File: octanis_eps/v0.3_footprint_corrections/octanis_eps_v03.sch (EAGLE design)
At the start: 100 parts, among them IC1 OPA2333DGK, IC5 OPA2333DGK, IC7 OPA2333DGK, IC9 OPA2333DGK, Q1 FC-12M, Q2 N-HEXFET-2D_SOT232-, Q3 N-HEXFET-2D_SOT232-, Q4 N-HEXFET-2D_SOT232-

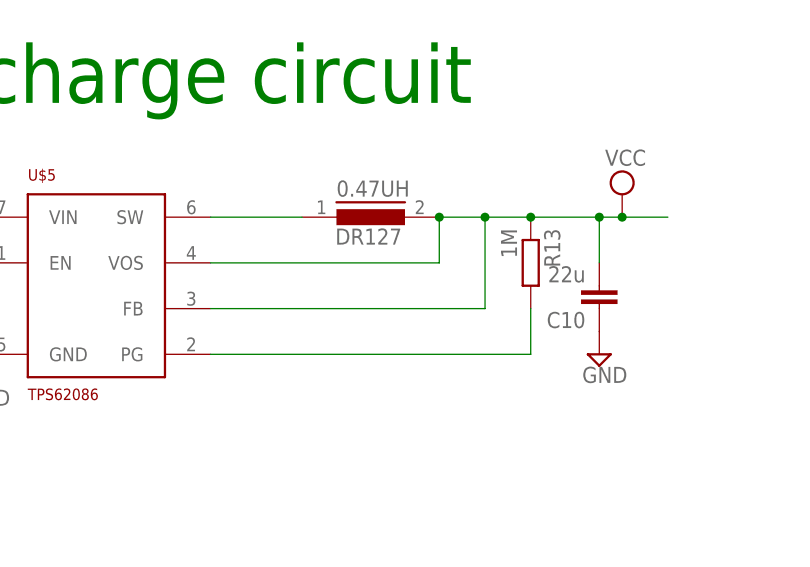
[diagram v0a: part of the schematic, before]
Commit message: corrected footprints for MSP & Step down, 50mOhms still to be changed (4points probe)
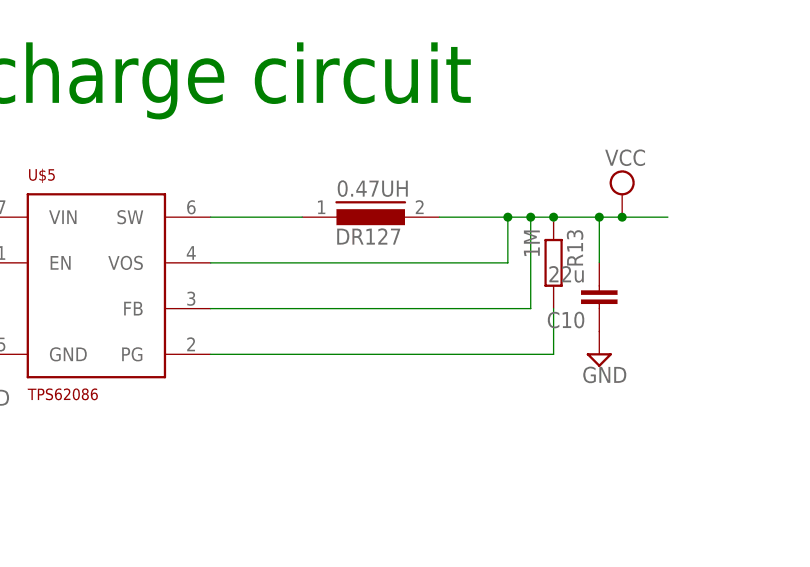
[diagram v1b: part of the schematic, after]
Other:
- moved on the sheet: R13
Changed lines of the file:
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@@
 <layer number="51" name="tDocu" color="7" fill="1" visible="no" active="no"/>
 <layer number="52" name="bDocu" color="7" fill="1" visible="no" active="no"/>
+<layer number="53" name="tGND_GNDA" color="7" fill="9" visible="no" active="no"/>
+<layer number="54" name="bGND_GNDA" color="1" fill="9" visible="no" active="no"/>
+<layer number="56" name="wert" color="7" fill="1" visible="no" active="no"/>
 <layer number="90" name="Modules" color="5" fill="1" visible="yes" active="yes"/>
 <layer number="91" name="Nets" color="2" fill="1" visible="yes" active="yes"/>
@@
 <layer number="109" name="fp9" color="7" fill="1" visible="yes" active="yes"/>
 <layer number="110" name="fp0" color="7" fill="1" visible="yes" active="yes"/>
+<layer number="111" name="LPC17xx" color="7" fill="1" visible="yes" active="yes"/>
+<layer number="112" name="tSilk" color="7" fill="1" visible="yes" active="yes"/>
 <layer number="116" name="Patch_BOT" color="9" fill="4" visible="yes" active="yes"/>
 <layer number="121" name="tTestdril" color="7" fill="1" visible="yes" active="yes"/>
@@
 <layer number="123" name="tTestmark" color="7" fill="1" visible="yes" active="yes"/>
 <layer number="124" name="bTestmark" color="7" fill="1" visible="yes" active="yes"/>
+<layer number="125" name="_tNames" color="7" fill="1" visible="yes" active="yes"/>
+<layer number="126" name="_bNames" color="7" fill="1" visible="yes" active="yes"/>
+<layer number="127" name="_tValues" color="7" fill="1" visible="yes" active="yes"/>
+<layer number="128" name="_bValues" color="7" fill="1" visible="yes" active="yes"/>
 <layer number="131" name="tAdjust" color="7" fill="1" visible="yes" active="yes"/>
 <layer number="132" name="bAdjust" color="7" fill="1" visible="yes" active="yes"/>
+<layer number="144" name="Drill_legend" color="7" fill="1" visible="yes" active="yes"/>
+<layer number="151" name="HeatSink" color="7" fill="1" visible="yes" active="yes"/>
+<layer number="152" name="_bDocu" color="7" fill="1" visible="yes" active="yes"/>
+<layer number="199" name="Contour" color="7" fill="1" visible="yes" active="yes"/>
 <layer number="200" name="200bmp" color="7" fill="1" visible="yes" active="yes"/>
 <layer number="201" name="201bmp" color="7" fill="1" visible="yes" active="yes"/>
@@
 <layer number="209" name="209bmp" color="7" fill="1" visible="yes" active="yes"/>
 <layer number="210" name="210bmp" color="7" fill="1" visible="yes" active="yes"/>
+<layer number="211" name="211bmp" color="7" fill="1" visible="yes" active="yes"/>
+<layer number="212" name="212bmp" color="7" fill="1" visible="yes" active="yes"/>
+<layer number="213" name="213bmp" color="7" fill="1" visible="yes" active="yes"/>
+<layer number="214" name="214bmp" color="7" fill="1" visible="yes" active="yes"/>
+<layer number="215" name="215bmp" color="7" fill="1" visible="yes" active="yes"/>
+<layer number="216" name="216bmp" color="7" fill="1" visible="yes" active="yes"/>
+<layer number="217" name="217bmp" color="18" fill="1" visible="no" active="no"/>
+<layer number="218" name="218bmp" color="19" fill="1" visible="no" active="no"/>
+<layer number="219" name="219bmp" color="20" fill="1" visible="no" active="no"/>
+<layer number="220" name="220bmp" color="21" fill="1" visible="no" active="no"/>
+<layer number="221" name="221bmp" color="22" fill="1" visible="no" active="no"/>
+<layer number="222" name="222bmp" color="23" fill="1" visible="no" active="no"/>
+<layer number="223" name="223bmp" color="24" fill="1" visible="no" active="no"/>
+<layer number="224" name="224bmp" color="25" fill="1" visible="no" active="no"/>
+<layer number="248" name="Housing" color="7" fill="1" visible="yes" active="yes"/>
+<layer number="249" name="Edge" color="7" fill="1" visible="yes" active="yes"/>
 <layer number="250" name="Descript" color="3" fill="1" visible="no" active="no"/>
 <layer number="251" name="SMDround" color="12" fill="11" visible="no" active="no"/>
@@
 <instance part="R11" gate="G$1" x="177.8" y="-182.88" rot="R180"/>
 <instance part="R12" gate="G$1" x="165.1" y="-167.64" rot="R270"/>
-<instance part="R13" gate="G$1" x="373.38" y="-167.64" rot="R270"/>
+<instance part="R13" gate="G$1" x="375.92" y="-167.64" rot="R270"/>
 <instance part="C4" gate="G$1" x="88.9" y="-177.8" rot="R180"/>
 <instance part="C5" gate="G$1" x="157.48" y="-193.04" rot="R180"/>
@@
 </segment>
 <segment>
-<pinref part="U$5" gate="G$1" pin="VOS"/>
-<wire x1="337.82" y1="-167.64" x2="363.22" y2="-167.64" width="0.1524" layer="91"/>
-<wire x1="363.22" y1="-167.64" x2="363.22" y2="-162.56" width="0.1524" layer="91"/>
 <pinref part="U$5" gate="G$1" pin="FB"/>
-<wire x1="337.82" y1="-172.72" x2="368.3" y2="-172.72" width="0.1524" layer="91"/>
-<wire x1="368.3" y1="-172.72" x2="368.3" y2="-162.56" width="0.1524" layer="91"/>
-<wire x1="368.3" y1="-162.56" x2="363.22" y2="-162.56" width="0.1524" layer="91"/>
-<wire x1="368.3" y1="-162.56" x2="373.38" y2="-162.56" width="0.1524" layer="91"/>
-<junction x="368.3" y="-162.56"/>
+<wire x1="337.82" y1="-172.72" x2="373.38" y2="-172.72" width="0.1524" layer="91"/>
+<wire x1="373.38" y1="-172.72" x2="373.38" y2="-162.56" width="0.1524" layer="91"/>
+<wire x1="373.38" y1="-162.56" x2="370.84" y2="-162.56" width="0.1524" layer="91"/>
+<wire x1="370.84" y1="-162.56" x2="363.22" y2="-162.56" width="0.1524" layer="91"/>
+<wire x1="373.38" y1="-162.56" x2="375.92" y2="-162.56" width="0.1524" layer="91"/>
+<junction x="373.38" y="-162.56"/>
 <pinref part="C10" gate="G$1" pin="2"/>
-<wire x1="373.38" y1="-162.56" x2="381" y2="-162.56" width="0.1524" layer="91"/>
+<wire x1="375.92" y1="-162.56" x2="381" y2="-162.56" width="0.1524" layer="91"/>
 <wire x1="381" y1="-167.64" x2="381" y2="-162.56" width="0.1524" layer="91"/>
 <wire x1="381" y1="-162.56" x2="383.54" y2="-162.56" width="0.1524" layer="91"/>
@@
 <junction x="383.54" y="-162.56"/>
 <pinref part="R13" gate="G$1" pin="1"/>
-<junction x="373.38" y="-162.56"/>
+<junction x="375.92" y="-162.56"/>
 <pinref part="0.47UH" gate="G$1" pin="2"/>
-<junction x="363.22" y="-162.56"/>
+<pinref part="U$5" gate="G$1" pin="VOS"/>
+<wire x1="337.82" y1="-167.64" x2="370.84" y2="-167.64" width="0.1524" layer="91"/>
+<wire x1="370.84" y1="-167.64" x2="370.84" y2="-162.56" width="0.1524" layer="91"/>
+<junction x="370.84" y="-162.56"/>
 </segment>
 <segment>
@@
 <pinref part="U$5" gate="G$1" pin="PG"/>
 <pinref part="R13" gate="G$1" pin="2"/>
-<wire x1="337.82" y1="-177.8" x2="373.38" y2="-177.8" width="0.1524" layer="91"/>
-<wire x1="373.38" y1="-177.8" x2="373.38" y2="-172.72" width="0.1524" layer="91"/>
-</segment>
-</net>
+<wire x1="337.82" y1="-177.8" x2="375.92" y2="-177.8" width="0.1524" layer="91"/>
+<wire x1="375.92" y1="-177.8" x2="375.92" y2="-172.72" width="0.1524" layer="91"/>
+</segment>
+</net>

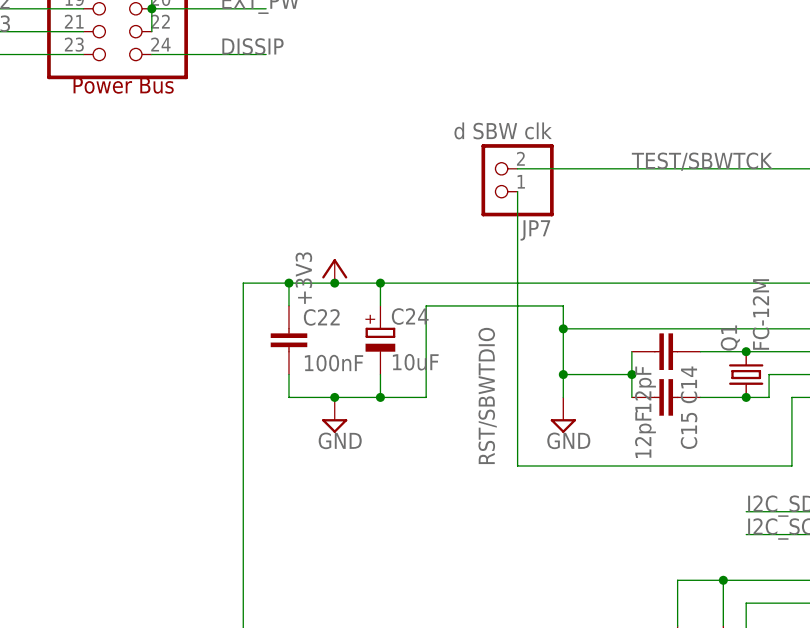
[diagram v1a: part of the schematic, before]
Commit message: pull-up on RST, need to modify the current sensor pads
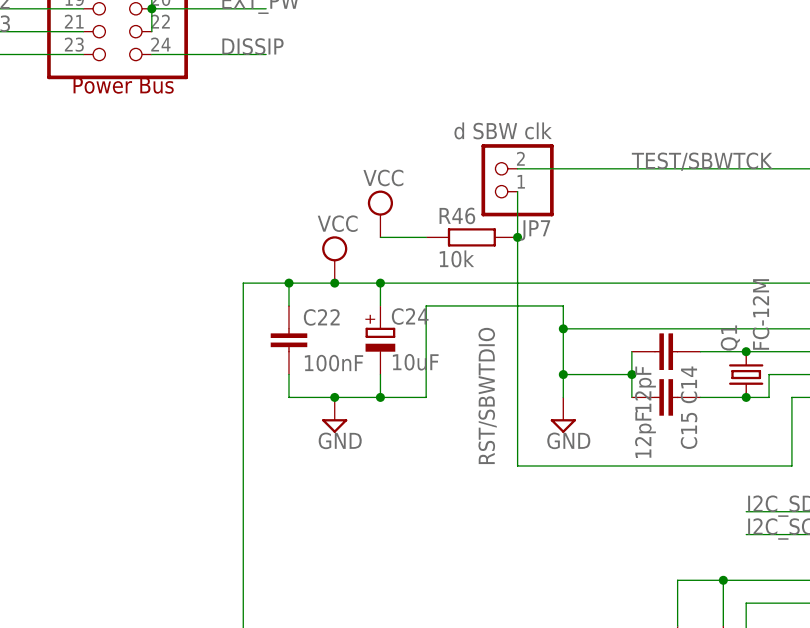
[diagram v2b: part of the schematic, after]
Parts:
- added R46: 10k, rcl:R-EU_R0603
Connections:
- removed net +3V3: C22.1, C24.+, FERRITE_BEAD.1, U$6.DVCC
- net RST/SBWTDIO: now also R46.2
- net VCC: now also C22.1, C24.+, FERRITE_BEAD.1, R46.1, U$6.DVCC
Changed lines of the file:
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@@
 <part name="SUPPLY41" library="supply2" deviceset="VCC" device=""/>
 <part name="SUPPLY42" library="supply2" deviceset="GND" device=""/>
-<part name="+3V3" library="supply1" deviceset="+3V3" device=""/>
 <part name="SUPPLY58" library="supply2" deviceset="GND" device=""/>
 <part name="SUPPLY66" library="supply2" deviceset="VCC" device=""/>
@@
 <part name="SUPPLY54" library="supply2" deviceset="GND" device=""/>
 <part name="R45" library="rcl" deviceset="R-EU_" device="R0603" value="0Ohm"/>
+<part name="R46" library="rcl" deviceset="R-EU_" device="R0603" value="10k"/>
+<part name="SUPPLY55" library="supply2" deviceset="VCC" device=""/>
+<part name="SUPPLY56" library="supply2" deviceset="VCC" device=""/>
 </parts>
 <sheets>
@@
 <instance part="SUPPLY41" gate="G$1" x="101.6" y="88.9"/>
 <instance part="SUPPLY42" gate="GND" x="101.6" y="22.86"/>
-<instance part="+3V3" gate="G$1" x="261.62" y="45.72"/>
 <instance part="SUPPLY58" gate="GND" x="261.62" y="27.94"/>
 <instance part="SUPPLY66" gate="G$1" x="81.28" y="-127"/>
@@
 <instance part="SUPPLY54" gate="GND" x="-33.02" y="50.8"/>
 <instance part="R45" gate="G$1" x="299.72" y="-167.64" rot="R270"/>
+<instance part="R46" gate="G$1" x="276.86" y="48.26"/>
+<instance part="SUPPLY55" gate="G$1" x="261.62" y="45.72"/>
+<instance part="SUPPLY56" gate="G$1" x="266.7" y="50.8"/>
 </instances>
 <busses>
@@
 <wire x1="66.04" y1="-195.58" x2="66.04" y2="-198.12" width="0.1524" layer="91"/>
 </segment>
+<segment>
+<wire x1="266.7" y1="43.18" x2="261.62" y2="43.18" width="0.1524" layer="91"/>
+<pinref part="C22" gate="G$1" pin="1"/>
+<wire x1="261.62" y1="43.18" x2="256.54" y2="43.18" width="0.1524" layer="91"/>
+<wire x1="256.54" y1="43.18" x2="256.54" y2="40.64" width="0.1524" layer="91"/>
+<pinref part="C24" gate="G$1" pin="+"/>
+<wire x1="266.7" y1="40.64" x2="266.7" y2="43.18" width="0.1524" layer="91"/>
+<junction x="266.7" y="43.18"/>
+<pinref part="U$6" gate="G$1" pin="DVCC"/>
+<wire x1="330.2" y1="43.18" x2="266.7" y2="43.18" width="0.1524" layer="91"/>
+<pinref part="FERRITE_BEAD" gate="G$1" pin="1"/>
+<wire x1="264.16" y1="-2.54" x2="251.46" y2="-2.54" width="0.1524" layer="91"/>
+<wire x1="251.46" y1="-2.54" x2="251.46" y2="43.18" width="0.1524" layer="91"/>
+<wire x1="251.46" y1="43.18" x2="256.54" y2="43.18" width="0.1524" layer="91"/>
+<junction x="256.54" y="43.18"/>
+<pinref part="SUPPLY55" gate="G$1" pin="VCC"/>
+<junction x="261.62" y="43.18"/>
+</segment>
+<segment>
+<pinref part="R46" gate="G$1" pin="1"/>
+<wire x1="266.7" y1="48.26" x2="271.78" y2="48.26" width="0.1524" layer="91"/>
+<pinref part="SUPPLY56" gate="G$1" pin="VCC"/>
+</segment>
 </net>
 <net name="VREF" class="0">
@@
 </segment>
 </net>
-<net name="+3V3" class="0">
-<segment>
-<pinref part="+3V3" gate="G$1" pin="+3V3"/>
-<wire x1="266.7" y1="43.18" x2="261.62" y2="43.18" width="0.1524" layer="91"/>
-<wire x1="261.62" y1="43.18" x2="256.54" y2="43.18" width="0.1524" layer="91"/>
-<junction x="261.62" y="43.18"/>
-<pinref part="C22" gate="G$1" pin="1"/>
-<wire x1="256.54" y1="43.18" x2="256.54" y2="40.64" width="0.1524" layer="91"/>
-<pinref part="C24" gate="G$1" pin="+"/>
-<wire x1="266.7" y1="40.64" x2="266.7" y2="43.18" width="0.1524" layer="91"/>
-<junction x="266.7" y="43.18"/>
-<pinref part="U$6" gate="G$1" pin="DVCC"/>
-<wire x1="330.2" y1="43.18" x2="266.7" y2="43.18" width="0.1524" layer="91"/>
-<pinref part="FERRITE_BEAD" gate="G$1" pin="1"/>
-<wire x1="264.16" y1="-2.54" x2="251.46" y2="-2.54" width="0.1524" layer="91"/>
-<wire x1="251.46" y1="-2.54" x2="251.46" y2="43.18" width="0.1524" layer="91"/>
-<wire x1="251.46" y1="43.18" x2="256.54" y2="43.18" width="0.1524" layer="91"/>
-<junction x="256.54" y="43.18"/>
-</segment>
-</net>
 <net name="N$45" class="0">
 <segment>
@@
 <label x="279.4" y="22.86" size="1.778" layer="95" rot="R90"/>
 <pinref part="JP7" gate="G$1" pin="1"/>
-<wire x1="281.94" y1="22.86" x2="281.94" y2="53.34" width="0.1524" layer="91"/>
+<wire x1="281.94" y1="22.86" x2="281.94" y2="48.26" width="0.1524" layer="91"/>
 <pinref part="U$6" gate="G$1" pin="RST/NMI/SBWTDIO"/>
+<wire x1="281.94" y1="48.26" x2="281.94" y2="53.34" width="0.1524" layer="91"/>
 <wire x1="330.2" y1="30.48" x2="312.42" y2="30.48" width="0.1524" layer="91"/>
 <wire x1="312.42" y1="30.48" x2="312.42" y2="22.86" width="0.1524" layer="91"/>
 <wire x1="312.42" y1="22.86" x2="281.94" y2="22.86" width="0.1524" layer="91"/>
-</segment>
-</net>
+<pinref part="R46" gate="G$1" pin="2"/>
+<junction x="281.94" y="48.26"/>
+</segment>
+</net>
